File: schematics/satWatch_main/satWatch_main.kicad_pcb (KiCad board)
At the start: 4 copper layers, 45.7 x 28 mm, 55 parts, among them J1 POGO_03x14, J2 Pogo_02x03_UARTPROG, Q1 DMP1045U, Q2 BSS138, Q3 BSS138, SW1 B3U-1000P, SW2 B3U-1000P, SW3 EVQ-P7A01P, SW4 EVQ-P7A01P, SW5 EVQ-P7A01P, U1 PAM2401SCADJ, U2 MIC5365-1.8YC5, U3 ESP32-S3-MINI-1, U4 MAX30101EFD_T, U5 BNO085, U6 DS3231MZ, Y1 32.768Hz

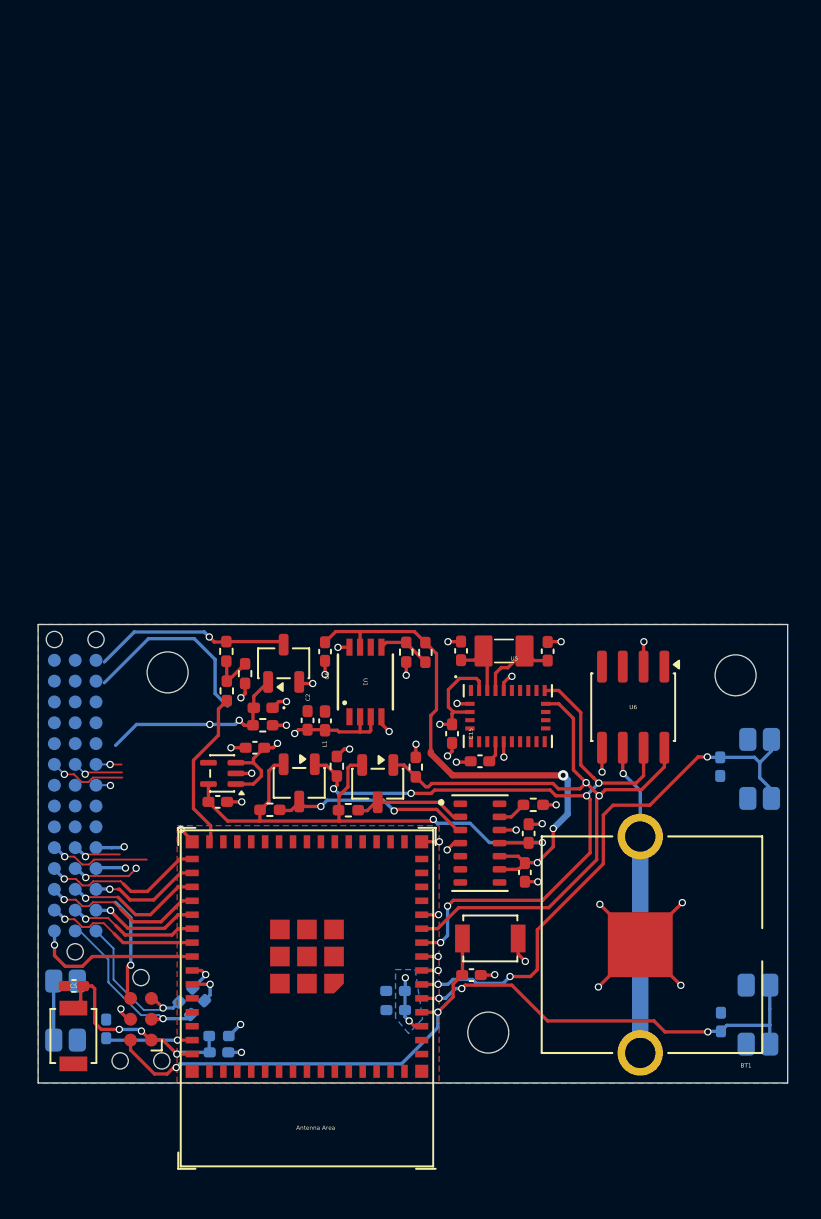
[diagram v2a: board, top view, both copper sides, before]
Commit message: v1
Completed large prototype testing. Implementing post-fab modifications into small-form board. Finalized mainboard routing iterations and added UART programming board.
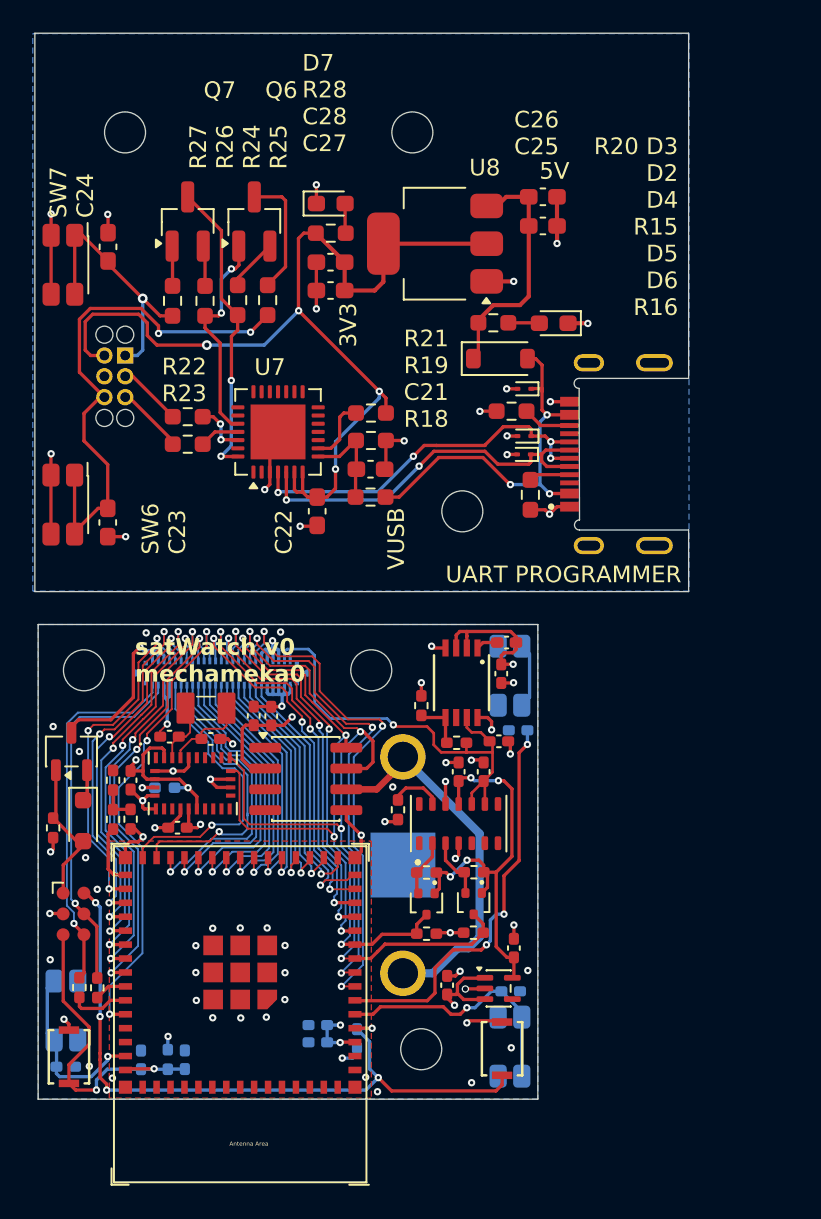
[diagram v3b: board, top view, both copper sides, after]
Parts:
- added C19: 10uF, Capacitor_SMD:C_0402_1005Metric_Pad0.74x0.62mm_HandSolder, F.Cu at (140.2, 81.8)
- added C20: 0.1uF, Capacitor_SMD:C_0402_1005Metric_Pad0.74x0.62mm_HandSolder, F.Cu at (141.2, 81.8)
- added C21: 1uF/16V, Capacitor_SMD:C_0603_1608Metric_Pad1.08x0.95mm_HandSolder, F.Cu at (147.3, 66.7)
- added C22: 10uF/25V, Capacitor_SMD:C_0603_1608Metric_Pad1.08x0.95mm_HandSolder, F.Cu at (144.0, 69.3)
- added C23: 0.1uF/50V, Capacitor_SMD:C_0603_1608Metric_Pad1.08x0.95mm_HandSolder, F.Cu at (131.2, 70.0)
- added C24: 0.1uF/50V, Capacitor_SMD:C_0603_1608Metric_Pad1.08x0.95mm_HandSolder, F.Cu at (131.3, 53.2)
- added C25: 10uF/25V, Capacitor_SMD:C_0603_1608Metric_Pad1.08x0.95mm_HandSolder, F.Cu at (157.8, 51.9)
- added C26: 0.1uF/50V, Capacitor_SMD:C_0603_1608Metric_Pad1.08x0.95mm_HandSolder, F.Cu at (157.8, 50.1)
- added C27: 10uF/25V, Capacitor_SMD:C_0603_1608Metric_Pad1.08x0.95mm_HandSolder, F.Cu at (144.8, 55.8)
- added C28: 0.1uF/50V, Capacitor_SMD:C_0603_1608Metric_Pad1.08x0.95mm_HandSolder, F.Cu at (144.8, 54.1)
- added D2: 1N5819, Diode_SMD:D_SOD-123, F.Cu at (155.2, 60.0)
- added D3: YELLOW, LED_SMD:LED_0603_1608Metric_Pad1.05x0.95mm_HandSolder, F.Cu at (158.4, 57.8)
- added D4: D5V0L1B2S9-7, Diode_SMD:D_SOD-923, F.Cu at (156.7, 61.8)
- added D5: D5V0L1B2S9-7, Diode_SMD:D_SOD-923, F.Cu at (156.7, 64.7)
- added D6: D5V0L1B2S9-7, Diode_SMD:D_SOD-923, F.Cu at (156.6, 65.8)
- added D7: RED, LED_SMD:LED_0603_1608Metric_Pad1.05x0.95mm_HandSolder, F.Cu at (144.8, 50.5)
- added H1: MountingHole, MountingHole:MountingHole_2.5mm, F.Cu at (149.8, 46.2)
- added H2: MountingHole, MountingHole:MountingHole_2.5mm, F.Cu at (132.3, 46.2)
- added H3: MountingHole, MountingHole:MountingHole_2.5mm, F.Cu at (152.9, 69.3)
- added J3: 855-22-006-10-001101, footprint:8552200610001101, B.Cu at (131.7, 61.1)
- added J4: UJ20-C-H-G-MSMT-2B-P16-TR, footprint:SAMESKY_UJ20-C-H-G-MSMT-2B-P16-TR, F.Cu at (163.4, 65.8)
- added Q6: S8050, Package_TO_SOT_SMD:SOT-23_Handsoldering, F.Cu at (140.2, 51.6)
- added Q7: S8050, Package_TO_SOT_SMD:SOT-23_Handsoldering, F.Cu at (136.1, 51.6)
- added R15: 5K, Resistor_SMD:R_0603_1608Metric_Pad0.98x0.95mm_HandSolder, F.Cu at (155.9, 63.2)
- added R16: 5K, Resistor_SMD:R_0603_1608Metric_Pad0.98x0.95mm_HandSolder, F.Cu at (157.0, 68.3)
- added R17: 10K, Resistor_SMD:R_0402_1005Metric_Pad0.72x0.64mm_HandSolder, B.Cu at (134.7, 86.2)
- added R18: 22.1K, Resistor_SMD:R_0603_1608Metric_Pad0.98x0.95mm_HandSolder, F.Cu at (147.3, 68.4)
- added R19: 47.5K, Resistor_SMD:R_0603_1608Metric_Pad0.98x0.95mm_HandSolder, F.Cu at (147.3, 65.0)
- added R20: 5.1K(1%), Resistor_SMD:R_0603_1608Metric_Pad0.98x0.95mm_HandSolder, F.Cu at (154.8, 57.8)
- added R21: 1K, Resistor_SMD:R_0603_1608Metric_Pad0.98x0.95mm_HandSolder, F.Cu at (147.3, 63.3)
- added R22: 0, Resistor_SMD:R_0603_1608Metric_Pad0.98x0.95mm_HandSolder, F.Cu at (136.1, 63.5)
- added R23: 0, Resistor_SMD:R_0603_1608Metric_Pad0.98x0.95mm_HandSolder, F.Cu at (136.1, 65.2)
- added R24: 10K, Resistor_SMD:R_0603_1608Metric_Pad0.98x0.95mm_HandSolder, F.Cu at (139.2, 56.4)
- added R25: 0, Resistor_SMD:R_0603_1608Metric_Pad0.98x0.95mm_HandSolder, F.Cu at (141.0, 56.4)
- added R26: 10K, Resistor_SMD:R_0603_1608Metric_Pad0.98x0.95mm_HandSolder, F.Cu at (137.2, 56.5)
- added R27: 0, Resistor_SMD:R_0603_1608Metric_Pad0.98x0.95mm_HandSolder, F.Cu at (135.2, 56.5)
- added R28: 5.1K, Resistor_SMD:R_0603_1608Metric_Pad0.98x0.95mm_HandSolder, F.Cu at (144.9, 52.3)
- added SW6: EVQ-P7A01P, Button_Switch_SMD:SW_SPST_EVQP7A, F.Cu at (128.5, 68.9)
- added SW7: EVQ-P7A01P, Button_Switch_SMD:SW_SPST_EVQP7A, F.Cu at (128.5, 54.3)
- added U7: CP2102N-Axx-xQFN28, Package_DFN_QFN:QFN-28-1EP_5x5mm_P0.5mm_EP3.35x3.35mm, F.Cu at (141.6, 64.5)
- added U8: AMS1117-3.3, Package_TO_SOT_SMD:SOT-223-3_TabPin2, F.Cu at (151.2, 53.0)
- BT1, C3, C5: moved to B.Cu
- D1: value SS34 -> SDB14HS-AQ; footprint Diode_SMD:D_0402_1005Metric_Pad0.77x0.64mm_HandSolder -> Diode_SMD:D_SOD-323_HandSoldering
- J1: value POGO_03x14 -> Conn_02x25_Top_Bottom; footprint footprint:CUSTOM_POGO_02X21 -> footprint:CON_2167010509_MOL
- Q2, Q3: value BSS138 -> RE1C002UN; footprint Package_TO_SOT_SMD:SOT-23-3 -> Package_TO_SOT_SMD:SOT-416
- R13: value 0 -> 499; moved to F.Cu
- R14: moved to F.Cu
- SW1, SW2: value B3U-1000P -> R-667995; footprint Button_Switch_SMD:SW_SPST_B3U-1000P -> footprint:R-667995_MIT-L
- moved H2 39.8 mm to (129.8, 79.0)
- moved U2 21.4 mm to (155.1, 98.4), turned to 0 degrees
- moved C17 21.2 mm to (137.5, 83.2), turned to 0 degrees
- moved U6 20.4 mm to (143.3, 85.6), turned to 0 degrees
- moved C4 20.1 mm to (156.0, 95.9), turned to 90 degrees
- moved C15 19.8 mm to (132.6, 85.7)
- moved U5 19.6 mm to (136.4, 85.9)
- moved C16 18.9 mm to (135.5, 88.6), turned to 0 degrees
- moved C1 18.6 mm to (151.9, 98.2), turned to 90 degrees
- moved C18 18.5 mm to (135.0, 83.0), turned to 180 degrees
- moved Y1 18.5 mm to (137.2, 81.3)
- moved SW5 16.3 mm to (155.8, 79.3)
- moved BT1 15.3 mm to (149.2, 90.9), turned to -90 degrees
- moved SW3 15.3 mm to (155.8, 102.0)
- moved R1 14.2 mm to (127.9, 88.6), turned to -90 degrees
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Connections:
- net /GPIO0/BOOT renamed /Mainboard/GPIO0/BOOT
- net /GPIO1/BUTTON1 renamed /Mainboard/GPIO1/BUTTON1
- net /GPIO2/BUTTON3 renamed /Mainboard/GPIO2/BUTTON3
- net /GPIO46/BUTTON2 renamed /Mainboard/GPIO46/BUTTON2
- C5 pad 1: /EN/CHIP_PU -> /Mainboard/EN/CHIP_PU
- C7 pad 1: /EN/CHIP_PU -> /Mainboard/EN/CHIP_PU
- J1 pad 1: /BAT+ -> /Mainboard/U0RXD
- J1 pad 10: unconnected-(J1-Pin_10-Pad10) -> /Mainboard/GPIO21
- J1 pad 11: /GPIO4 -> /Mainboard/GPIO20/USBD+
- J1 pad 12: /GPIO36 -> /Mainboard/GPIO19/USBD-
- J1 pad 13: /GPIO39 -> /Mainboard/GPIO18
- J1 pad 14: /U0TXD -> /Mainboard/GPIO17
- J1 pad 15: unconnected-(J1-Pin_15-Pad15) -> /Mainboard/GPIO16
- J1 pad 16: unconnected-(J1-Pin_16-Pad16) -> /Mainboard/GPIO15
- J1 pad 17: unconnected-(J1-Pin_17-Pad17) -> /Mainboard/GPIO14
- J1 pad 18: unconnected-(J1-Pin_18-Pad18) -> /Mainboard/GPIO13
- J1 pad 19: unconnected-(J1-Pin_19-Pad19) -> /Mainboard/GPIO12
- J1 pad 2: 3V3 -> /Mainboard/U0TXD
- J1 pad 20: unconnected-(J1-Pin_20-Pad20) -> /Mainboard/GPIO11
- J1 pad 21: unconnected-(J1-Pin_21-Pad21) -> GND
- J1 pad 22: unconnected-(J1-Pin_22-Pad22) -> GND
- J1 pad 23: unconnected-(J1-Pin_23-Pad23) -> GND
- J1 pad 24: unconnected-(J1-Pin_24-Pad24) -> GND
- J1 pad 25: /GPIO3 -> GND
- J1 pad 26: /GPIO37 -> /Mainboard/BAT+
- J1 pad 27: /GPIO40 -> /Mainboard/BAT+
- J1 pad 28: /U0RXD -> /Mainboard/BAT+
- J1 pad 29: unconnected-(J1-Pin_29-Pad29) -> /Mainboard/GPIO36
- J1 pad 3: unconnected-(J1-Pin_3-Pad3) -> GND
- J1 pad 30: unconnected-(J1-Pin_30-Pad30) -> /Mainboard/GPIO37
- J1 pad 31: unconnected-(J1-Pin_31-Pad31) -> /Mainboard/GPIO38
- J1 pad 32: unconnected-(J1-Pin_32-Pad32) -> /Mainboard/GPIO39
- J1 pad 33: unconnected-(J1-Pin_33-Pad33) -> /Mainboard/GPIO40
- J1 pad 34: unconnected-(J1-Pin_34-Pad34) -> /Mainboard/GPIO41
- J1 pad 35: unconnected-(J1-Pin_35-Pad35) -> /Mainboard/GPIO42
- J1 pad 36: unconnected-(J1-Pin_36-Pad36) -> /Mainboard/GPIO45
- J1 pad 37: unconnected-(J1-Pin_37-Pad37) -> /Mainboard/GPIO10
- J1 pad 38: /GPIO2 -> /Mainboard/GPIO9/MOSI
- J1 pad 39: /GPIO35 -> /Mainboard/GPIO8/MISO
- J1 pad 4: unconnected-(J1-Pin_4-Pad4) -> GND
- J1 pad 40: /GPIO38 -> /Mainboard/GPIO7/SCK
- J1 pad 41: /GPIO41 -> /Mainboard/GPIO6/SCL
- J1 pad 42: /GPIO42 -> /Mainboard/GPIO5/SDA
- J1 pad 5: unconnected-(J1-Pin_5-Pad5) -> /Mainboard/GPIO48
- J1 pad 6: unconnected-(J1-Pin_6-Pad6) -> /Mainboard/GPIO34
- J1 pad 7: unconnected-(J1-Pin_7-Pad7) -> /Mainboard/GPIO33
- J1 pad 8: unconnected-(J1-Pin_8-Pad8) -> /Mainboard/GPIO47
- J1 pad 9: unconnected-(J1-Pin_9-Pad9) -> /Mainboard/GPIO27
- J2 pad 1: /EN/CHIP_PU -> VIN_3V3
- J2 pad 2: /U0RXD -> GND
- J2 pad 3: /U0TXD -> /Mainboard/EN/CHIP_PU
- J2 pad 4: VIN_3V3 -> /Mainboard/U0RXD
- J2 pad 5: GND -> /Mainboard/U0TXD
- Q1 pad 3: /BAT+ -> /Mainboard/BAT+
- Q2 pad 1: /GPIO6/SCL -> 1V8
- Q2 pad 2: 1V8 -> /Mainboard/LV_SCL
- Q2 pad 3: /LV_SCL -> /Mainboard/GPIO6/SCL
- Q3 pad 1: /GPIO5/SDA -> 1V8
- Q3 pad 2: 1V8 -> /Mainboard/LV_SDA
- Q3 pad 3: /LV_SDA -> /Mainboard/GPIO5/SDA
- R11 pad 2: /GPIO5/SDA -> /Mainboard/GPIO5/SDA
- R13 pad 2: /U0TXD -> /Mainboard/U0TXD
- R14 pad 2: /U0RXD -> /Mainboard/U0RXD
- R4 pad 2: /LV_SCL -> /Mainboard/LV_SCL
- R5 pad 2: /EN/CHIP_PU -> /Mainboard/EN/CHIP_PU
- R6 pad 2: /GPIO6/SCL -> /Mainboard/GPIO6/SCL
- R7 pad 1: /GPIO48/BATTERY_MONITOR -> /Mainboard/GPIO35/BATTERY_MONITOR
- R8 pad 2: /BAT+ -> /Mainboard/BAT+
- R9 pad 2: /LV_SDA -> /Mainboard/LV_SDA
- SW2 pad 2: /EN/CHIP_PU -> /Mainboard/EN/CHIP_PU
- U3 pad 10: /GPIO6/SCL -> /Mainboard/GPIO6/SCL
- U3 pad 11: /GPIO7/SCK -> /Mainboard/GPIO7/SCK
- U3 pad 12: /GPIO8/MISO -> /Mainboard/GPIO8/MISO
- U3 pad 13: /GPIO9/MOSI -> /Mainboard/GPIO9/MOSI
- U3 pad 14: /GPIO10 -> /Mainboard/GPIO10
- U3 pad 15: /GPIO11 -> /Mainboard/GPIO11
- U3 pad 16: /GPIO12 -> /Mainboard/GPIO12
- U3 pad 17: /GPIO13 -> /Mainboard/GPIO13
- U3 pad 18: /GPIO14 -> /Mainboard/GPIO14
- U3 pad 19: /GPIO15 -> /Mainboard/GPIO15
- U3 pad 20: /GPIO16 -> /Mainboard/GPIO16
- U3 pad 21: /GPIO17 -> /Mainboard/GPIO17
- U3 pad 22: /GPIO18 -> /Mainboard/GPIO18
- U3 pad 23: /GPIO19/USBD- -> /Mainboard/GPIO19/USBD-
- U3 pad 24: /GPIO20/USBD+ -> /Mainboard/GPIO20/USBD+
- U3 pad 25: /GPIO21 -> /Mainboard/GPIO21
- U3 pad 26: /GPIO27 -> /Mainboard/GPIO27
- U3 pad 27: /GPIO47 -> /Mainboard/GPIO47
- U3 pad 28: /GPIO33 -> /Mainboard/GPIO33
- U3 pad 29: /GPIO34 -> /Mainboard/GPIO34
- U3 pad 30: /GPIO48/BATTERY_MONITOR -> /Mainboard/GPIO48
- U3 pad 31: /GPIO35 -> /Mainboard/GPIO35/BATTERY_MONITOR
- U3 pad 32: /GPIO36 -> /Mainboard/GPIO36
- U3 pad 33: /GPIO37 -> /Mainboard/GPIO37
- U3 pad 34: /GPIO38 -> /Mainboard/GPIO38
- U3 pad 35: /GPIO39 -> /Mainboard/GPIO39
- U3 pad 36: /GPIO40 -> /Mainboard/GPIO40
- U3 pad 37: /GPIO41 -> /Mainboard/GPIO41
- U3 pad 38: /GPIO42 -> /Mainboard/GPIO42
- U3 pad 41: /GPIO45 -> /Mainboard/GPIO45
- U3 pad 45: /EN/CHIP_PU -> /Mainboard/EN/CHIP_PU
- U3 pad 7: /GPIO3 -> /Mainboard/GPIO3
- U3 pad 8: /GPIO4 -> /Mainboard/GPIO4
- U3 pad 9: /GPIO5/SDA -> /Mainboard/GPIO5/SDA
- U4 pad 2: /LV_SCL -> /Mainboard/LV_SCL
- U4 pad 3: /LV_SDA -> /Mainboard/LV_SDA
- U5 pad 11: unconnected-(U5-~{RST}-Pad11) -> 3V3
- U5 pad 17: unconnected-(U5-SA0/H_MOSI-Pad17) -> GND
- U5 pad 18: unconnected-(U5-~{H_CS}-Pad18) -> GND
- U5 pad 19: /GPIO6/SCL -> /Mainboard/GPIO6/SCL
- U5 pad 20: /GPIO5/SDA -> /Mainboard/GPIO5/SDA
- U5 pad 4: unconnected-(U5-~{BOOT}-Pad4) -> Net-(U5-~{BOOT})
- U5 pad 5: unconnected-(U5-PS1-Pad5) -> GND
- U5 pad 6: unconnected-(U5-PS0/WAKE-Pad6) -> GND
- U6 pad 7: /GPIO5/SDA -> /Mainboard/GPIO5/SDA
- U6 pad 8: /GPIO6/SCL -> /Mainboard/GPIO6/SCL
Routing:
- net PROG_3V3: track 0.00 -> 60.1 mm, vias 0 -> 4
- net /Mainboard/GPIO5/SDA: track 0.00 -> 52.6 mm, vias 0 -> 4
- net /GPIO5/SDA: track 49.6 -> 0.00 mm, vias 6 -> 0
- net /GPIO6/SCL: track 42.4 -> 0.00 mm, vias 2 -> 0
- net /Mainboard/GPIO6/SCL: track 0.00 -> 41.6 mm, vias 0 -> 4
- net PROG_GND: track 0.00 -> 36.3 mm, vias 0 -> 18
- net /Programmer/EN/CHIP_PU: track 0.00 -> 32.9 mm, vias 0 -> 2
- net /Mainboard/GPIO3: track 0.00 -> 31.3 mm, vias 0 -> 3
- net /Mainboard/GPIO45: track 0.00 -> 29.8 mm, vias 0 -> 3
- net /Mainboard/GPIO4: track 0.00 -> 29.1 mm, vias 0 -> 3
- net /Mainboard/GPIO42: track 0.00 -> 26.2 mm, vias 0 -> 3
- net /Mainboard/GPIO41: track 0.00 -> 26.0 mm, vias 0 -> 3
- net /Mainboard/GPIO7/SCK: track 0.00 -> 25.1 mm, vias 0 -> 3
- net /Mainboard/GPIO40: track 0.00 -> 24.3 mm, vias 0 -> 3
- net /Mainboard/GPIO39: track 0.00 -> 24.1 mm, vias 0 -> 3
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- added copper zone on In2.Cu, net PROG_3V3
- added copper zone on B.Cu, net PROG_GND
- added copper zone on In1.Cu, net PROG_GND
- removed copper zone on B.Cu, net (none)
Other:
- board size 45.7 x 28 mm -> 39.9 x 65 mm
- board text added: "3V3"
- board text added: "5V"
- board text added: "BOOT 3V3 TX GND RX EN"
- board text added: "C22"
- board text added: "C26 C25"
- board text added: "D7 R28 C28 C27"
- board text added: "MAINBOARD"
- board text added: "Q7 Q6"
- board text added: "R20 D3 D2 D4 R15 D5 D6 R16"
- board text added: "R21 R19 C21 R18"
- board text added: "R22 R23"
- board text added: "R27 R26 R24 R25"
- board text added: "SW6 C23"
- board text added: "SW7 C24"
- board text added: "U7"
- board text added: "U8"
- board text added: "UART PROGRAMMER"
- board text added: "VUSB"
- board text added: "satWatch v0 mechameka0"

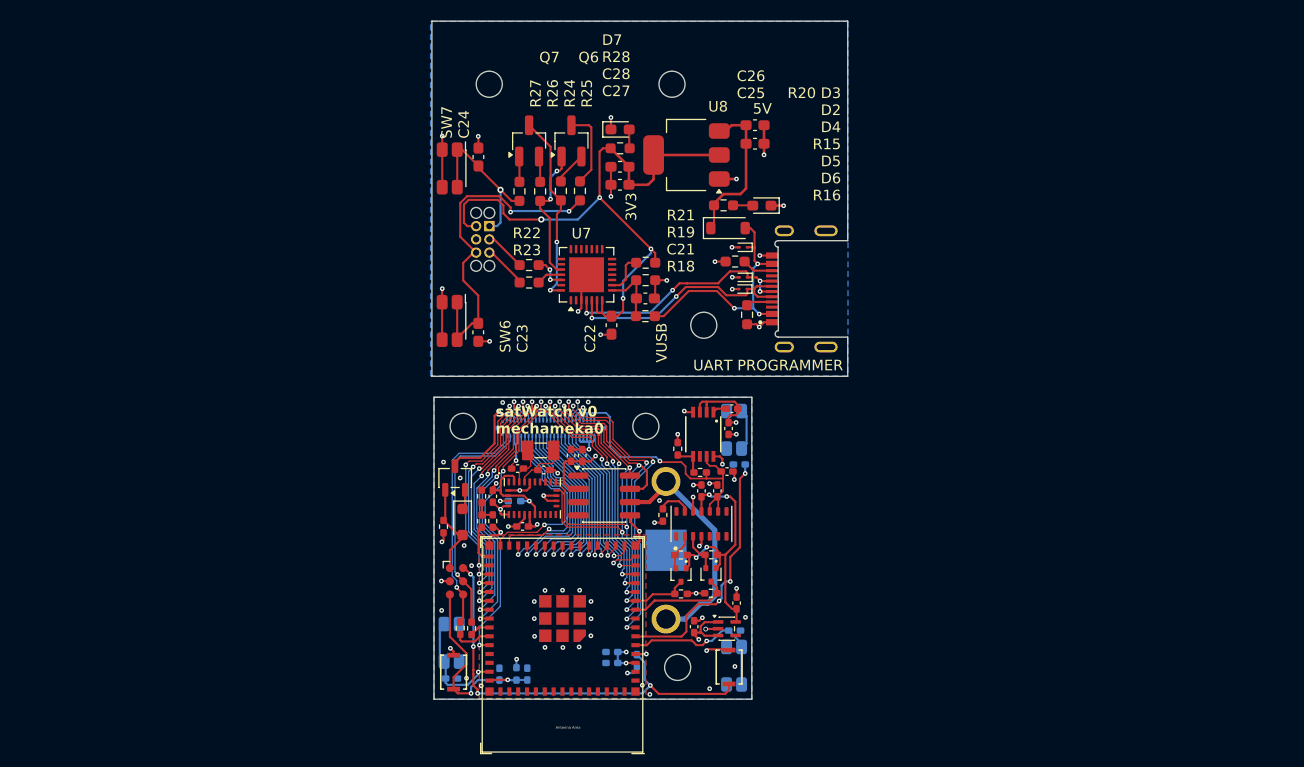
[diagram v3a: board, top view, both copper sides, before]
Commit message: v1.1
Completed board layout for charging dock configuration and a default watchface config
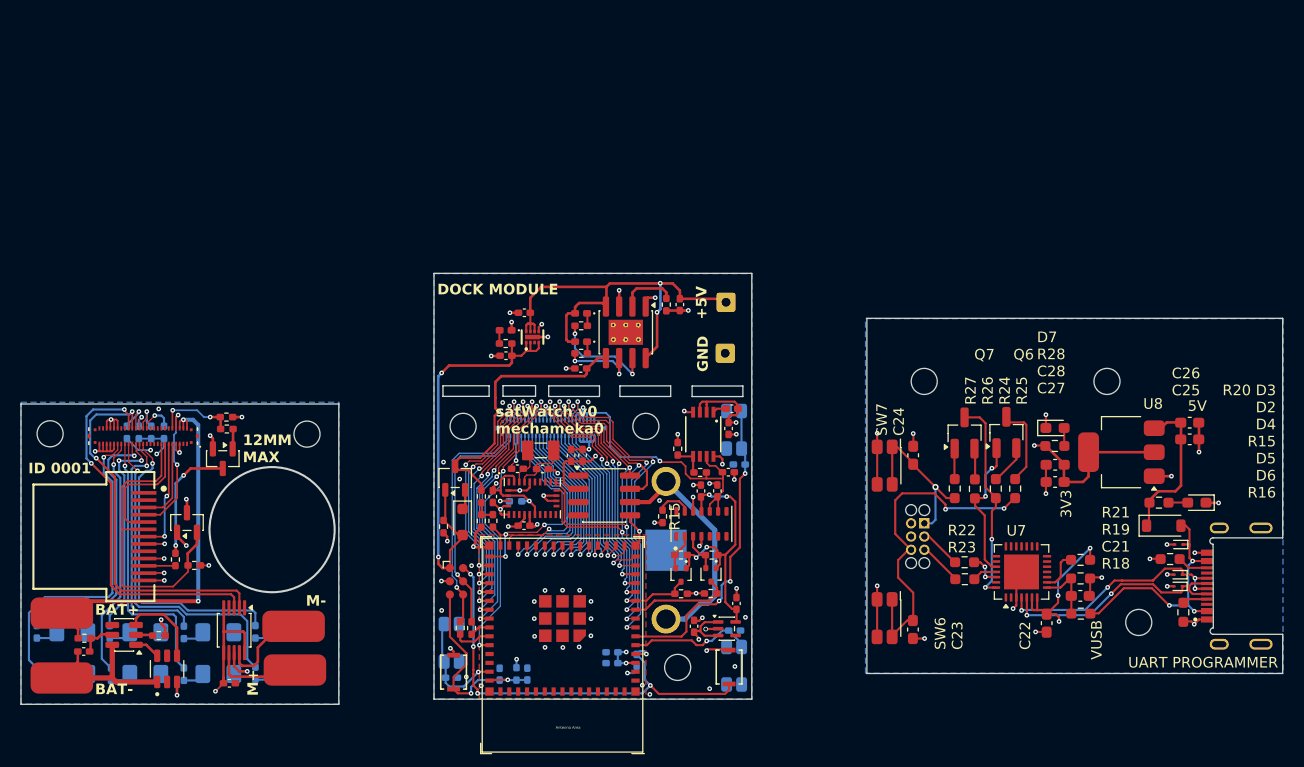
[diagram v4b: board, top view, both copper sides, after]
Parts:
- added C29: 0.1uF, Capacitor_SMD:C_0402_1005Metric_Pad0.74x0.62mm_HandSolder, F.Cu at (150.6, 67.3)
- added C30: 10uF, Capacitor_SMD:C_0402_1005Metric_Pad0.74x0.62mm_HandSolder, F.Cu at (141.1, 73.4)
- added C31: 1uF, Capacitor_SMD:C_0402_1005Metric_Pad0.74x0.62mm_HandSolder, F.Cu at (135.7, 68.1)
- added C32: 1uF, Capacitor_SMD:C_0402_1005Metric_Pad0.74x0.62mm_HandSolder, F.Cu at (133.9, 72.2)
- added C33: 1uF, Capacitor_SMD:C_0402_1005Metric_Pad0.74x0.62mm_HandSolder, F.Cu at (107.4, 103.6)
- added C34: 0.1uF, Capacitor_SMD:C_0402_1005Metric_Pad0.74x0.62mm_HandSolder, F.Cu at (93.4, 100.6)
- added D10: RED, LED_SMD:LED_0402_1005Metric_Pad0.77x0.64mm_HandSolder, F.Cu at (133.9, 69.8)
- added D11: LED, LED_SMD:LED_1206_3216Metric_Pad1.42x1.75mm_HandSolder, B.Cu at (113.3, 98.7)
- added D12: LED, LED_SMD:LED_1206_3216Metric_Pad1.42x1.75mm_HandSolder, B.Cu at (106.3, 98.7)
- added D13: LED, LED_SMD:LED_1206_3216Metric_Pad1.42x1.75mm_HandSolder, B.Cu at (99.3, 98.7)
- added D14: LED, LED_SMD:LED_1206_3216Metric_Pad1.42x1.75mm_HandSolder, B.Cu at (92.3, 98.7)
- added D15: LED, LED_SMD:LED_1206_3216Metric_Pad1.42x1.75mm_HandSolder, B.Cu at (113.3, 102.7)
- added D16: LED, LED_SMD:LED_1206_3216Metric_Pad1.42x1.75mm_HandSolder, B.Cu at (106.3, 102.7)
- added D17: LED, LED_SMD:LED_1206_3216Metric_Pad1.42x1.75mm_HandSolder, B.Cu at (99.3, 102.7)
- added D18: LED, LED_SMD:LED_1206_3216Metric_Pad1.42x1.75mm_HandSolder, B.Cu at (92.3, 102.7)
- added D8: DONE, LED_SMD:LED_0402_1005Metric_Pad0.77x0.64mm_HandSolder, F.Cu at (141.1, 70.9)
- added D9: CHRG, LED_SMD:LED_0402_1005Metric_Pad0.77x0.64mm_HandSolder, F.Cu at (141.1, 68.2)
- added H1: MountingHole, MountingHole:MountingHole_2.5mm, F.Cu at (114.8, 79.7)
- added H2: MountingHole, MountingHole:MountingHole_2.5mm, F.Cu at (90.2, 79.7)
- added J10: BAT+, Connector_Wire:SolderWirePad_1x01_SMD_3x6mm, F.Cu at (91.3, 96.9)
- added J11: BAT-, Connector_Wire:SolderWirePad_1x01_SMD_3x6mm, F.Cu at (91.3, 103.1)
- added J5: SOLDER POINT, Connector_Wire:SolderWire-0.25sqmm_1x01_D0.65mm_OD1.7mm, F.Cu at (155.0, 67.1)
- added J6: SOLDER POINT, Connector_Wire:SolderWire-0.25sqmm_1x01_D0.65mm_OD1.7mm, F.Cu at (154.9, 72.0)
- added J7: 2167010509_MOLEX, footprint:CON_2167010509_MOL, F.Cu at (99.1, 79.9)
- added J8: MOTOR+, Connector_Wire:SolderWirePad_1x01_SMD_3x6mm, F.Cu at (113.7, 102.4)
- added J9: MOTOR-, Connector_Wire:SolderWirePad_1x01_SMD_3x6mm, F.Cu at (113.5, 98.2)
- added Q4: S8050, Package_TO_SOT_SMD:SOT-23_Handsoldering, F.Cu at (181.9, 79.6)
- added Q5: S8050, Package_TO_SOT_SMD:SOT-23_Handsoldering, F.Cu at (177.9, 79.6)
- added R29: 1K, Resistor_SMD:R_0402_1005Metric_Pad0.72x0.64mm_HandSolder, F.Cu at (141.1, 72.0)
- added R30: 1K, Resistor_SMD:R_0402_1005Metric_Pad0.72x0.64mm_HandSolder, F.Cu at (141.1, 69.4)
- added R31: 1.2k, Resistor_SMD:R_0402_1005Metric_Pad0.72x0.64mm_HandSolder, F.Cu at (149.3, 67.3)
- added R32: 5.1K(1%), Resistor_SMD:R_0402_1005Metric_Pad0.72x0.64mm_HandSolder, F.Cu at (133.9, 71.1)
- added R33: 1K, Resistor_SMD:R_0402_1005Metric_Pad0.72x0.64mm_HandSolder, F.Cu at (107.1, 79.2)
- added R34: 22, Resistor_SMD:R_0402_1005Metric_Pad0.72x0.64mm_HandSolder, F.Cu at (102.2, 91.8)
- added R35: 10K, Resistor_SMD:R_0402_1005Metric_Pad0.72x0.64mm_HandSolder, F.Cu at (107.1, 78.1)
- added R36: 10K, Resistor_SMD:R_0402_1005Metric_Pad0.72x0.64mm_HandSolder, F.Cu at (104.0, 92.3)
- added R37: 180, Resistor_SMD:R_0402_1005Metric_Pad0.72x0.64mm_HandSolder, B.Cu at (109.9, 98.7)
- added R38: 180, Resistor_SMD:R_0402_1005Metric_Pad0.72x0.64mm_HandSolder, B.Cu at (103.0, 98.7)
- added R39: 180, Resistor_SMD:R_0402_1005Metric_Pad0.72x0.64mm_HandSolder, B.Cu at (95.9, 98.7)
- added R40: 180, Resistor_SMD:R_0402_1005Metric_Pad0.72x0.64mm_HandSolder, B.Cu at (88.9, 98.7)
- added R41: 180, Resistor_SMD:R_0402_1005Metric_Pad0.72x0.64mm_HandSolder, B.Cu at (109.9, 102.7)
- added R42: 180, Resistor_SMD:R_0402_1005Metric_Pad0.72x0.64mm_HandSolder, B.Cu at (103.0, 102.8)
- added R43: 180, Resistor_SMD:R_0402_1005Metric_Pad0.72x0.64mm_HandSolder, B.Cu at (96.0, 102.8)
- added R44: 180, Resistor_SMD:R_0402_1005Metric_Pad0.72x0.64mm_HandSolder, B.Cu at (88.9, 102.8)
- added R45: 100, Resistor_SMD:R_0402_1005Metric_Pad0.72x0.64mm_HandSolder, F.Cu at (93.5, 99.3)
- added R46: 1K, Resistor_SMD:R_0402_1005Metric_Pad0.72x0.64mm_HandSolder, F.Cu at (100.6, 99.1)
- added R47: 10K, Resistor_SMD:R_0402_1005Metric_Pad0.72x0.64mm_HandSolder, B.Cu at (97.6, 79.6)
- added R48: 10K, Resistor_SMD:R_0402_1005Metric_Pad0.72x0.64mm_HandSolder, B.Cu at (98.7, 79.6)
- added R49: 10K, Resistor_SMD:R_0402_1005Metric_Pad0.72x0.64mm_HandSolder, B.Cu at (99.9, 79.6)
- added R50: 10K, Resistor_SMD:R_0402_1005Metric_Pad0.72x0.64mm_HandSolder, B.Cu at (101.1, 79.6)
- added U10: NCP186AMX330TAG, footprint:PSON40P160X120X45-9N, F.Cu at (136.4, 70.4)
- added U11: ~, footprint:Wisevision N096-1608TBBIG11-H13, F.Cu at (99.2, 89.6)
- added U12: ~, Package_TO_SOT_SMD:SOT-23, F.Cu at (103.3, 88.2)
- added U13: DRV2605LDGS, Package_SO:TSSOP-10_3x3mm_P0.5mm, F.Cu at (107.8, 98.5)
- added U14: DW01A, Package_TO_SOT_SMD:SOT-23-6, F.Cu at (97.3, 99.0)
- added U9: TP4056-42-ESOP8, Package_SO:SOIC-8-1EP_3.9x4.9mm_P1.27mm_EP2.41x3.3mm_ThermalVias, F.Cu at (145.4, 70.0)
- C12: value 0.1uF/50V(10%) -> 0.1uF; moved to F.Cu
- C13: value 0.1uF -> 0.1uF/50V(10%); moved to B.Cu
- C17: value 22pF -> 10uF
- C19: value 10uF -> 0.1uF
- C20: value 0.1uF -> 22pF
- C21: value 1uF/16V -> 10uF/25V
- C22, C27: value 10uF/25V -> 0.1uF/50V
- C23, C26: value 0.1uF/50V -> 10uF/25V
- C25: value 10uF/25V -> 1uF/16V
- C3: value 0.1uF/50V(10%) -> 1uF; moved to F.Cu
- C4: value 1uF -> 22uF
- C5: value 0.1uF/50V(10%) -> 1uF/16V(10%)
- C6: value 22uF -> 10uF/16V(10%); moved to B.Cu
- C8: value 1uF/16V(10%) -> 0.1uF/50V(10%)
- C9: value 10uF/16V(10%) -> 0.1uF/50V(10%)
- D2: value 1N5819 -> D5V0L1B2S9-7; footprint Diode_SMD:D_SOD-123 -> Diode_SMD:D_SOD-923
- D3: value YELLOW -> D5V0L1B2S9-7; footprint LED_SMD:LED_0603_1608Metric_Pad1.05x0.95mm_HandSolder -> Diode_SMD:D_SOD-923
- D4: value D5V0L1B2S9-7 -> 1N5819; footprint Diode_SMD:D_SOD-923 -> Diode_SMD:D_SOD-123
- D6: value D5V0L1B2S9-7 -> RED; footprint Diode_SMD:D_SOD-923 -> LED_SMD:LED_0603_1608Metric_Pad1.05x0.95mm_HandSolder
- D7: value RED -> YELLOW
- J1: value Conn_02x25_Top_Bottom -> 2167010509_MOLEX
- Q6: value S8050 -> MMBT2222A; footprint Package_TO_SOT_SMD:SOT-23_Handsoldering -> Package_TO_SOT_SMD:SOT-23
- Q7: value S8050 -> FS8205; footprint Package_TO_SOT_SMD:SOT-23_Handsoldering -> footprint:SOT95P280X145-6N
- R12: value 4.7K -> 220K
- R13: value 499 -> 2.2K
- R14: value 0 -> 10K; moved to B.Cu
- R15: value 5K -> 4.7K; footprint Resistor_SMD:R_0603_1608Metric_Pad0.98x0.95mm_HandSolder -> Resistor_SMD:R_0402_1005Metric_Pad0.72x0.64mm_HandSolder
- R17: value 10K -> 5K; footprint Resistor_SMD:R_0402_1005Metric_Pad0.72x0.64mm_HandSolder -> Resistor_SMD:R_0603_1608Metric_Pad0.98x0.95mm_HandSolder; moved to F.Cu
- R18: value 22.1K -> 5.1K
- R19: value 47.5K -> 5.1K(1%)
- R20: value 5.1K(1%) -> 22.1K
- R21: value 1K -> 47.5K
- R22: value 0 -> 1K
- R23: value 0 -> 10K
- R26: value 10K -> 0
- R28: value 5.1K -> 0
- R6: value 2.2K -> 499
- R8: value 220K -> 2.2K
- R9: value 2.2K -> 0
- moved D7 65.9 mm to (200.2, 86.3), turned to 180 degrees
- moved R17 65.0 mm to (198.9, 96.8), turned to -90 degrees
- moved C24 63.5 mm to (186.6, 84.3), turned to 180 degrees
- moved Q7 61.4 mm to (101.4, 102.2)
- moved R22 60.0 mm to (189.0, 91.8)
- moved C23 56.8 mm to (186.6, 82.7), turned to 180 degrees
- moved C22 56.2 mm to (199.5, 78.6), turned to 0 degrees
- moved R27 55.4 mm to (182.7, 85.0)
- moved C26 55.3 mm to (185.8, 97.9), turned to 90 degrees
- moved R26 55.2 mm to (177.9, 93.7), turned to 0 degrees
- moved C21 53.9 mm to (199.5, 80.2)
- moved R19 53.7 mm to (196.5, 86.3), turned to 180 degrees
- moved C25 53.4 mm to (189.0, 95.3)
- moved D3 53.4 mm to (198.4, 93.2)
- moved D2 52.8 mm to (198.4, 90.3), turned to 180 degrees
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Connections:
- net /Mainboard/GPIO7/SCK renamed /Mainboard/GPIO7
- net /Mainboard/GPIO8/MISO renamed /Mainboard/GPIO8
- net /Mainboard/GPIO9/MOSI renamed /Mainboard/GPIO9
- C12 pad 1: /Mainboard/GPIO46/BUTTON2 -> 1V8
- C13 pad 1: 1V8 -> /Mainboard/GPIO46/BUTTON2
- C15 pad 1: 3V3 -> Net-(U5-CAP)
- C16 pad 1: Net-(U5-CAP) -> 3V3
- C17 pad 1: Net-(U5-XOUT32/CLKSEL1) -> 3V3
- C18 pad 1: Net-(U5-XIN32) -> Net-(U5-XOUT32/CLKSEL1)
- C20 pad 1: 3V3 -> Net-(U5-XIN32)
- C21 pad 1: Net-(U7-VBUS) -> PROG_5V
- C22 pad 1: PROG_GND -> PROG_5V
- C22 pad 2: PROG_3V3 -> PROG_GND
- C23 pad 1: /Programmer/EN/CHIP_PU -> PROG_3V3
- C24 pad 1: /Programmer/GPIO0/BOOT -> PROG_3V3
- C25 pad 1: PROG_5V -> Net-(U7-VBUS)
- C26 pad 1: PROG_5V -> PROG_GND
- C26 pad 2: PROG_GND -> PROG_3V3
- C27 pad 1: PROG_3V3 -> /Programmer/EN/CHIP_PU
- C28 pad 1: PROG_3V3 -> /Programmer/GPIO0/BOOT
- C3 pad 1: /Mainboard/GPIO0/BOOT -> 1V8
- C4 pad 1: 1V8 -> 5V
- C5 pad 1: /Mainboard/EN/CHIP_PU -> 3V3
- C6 pad 1: 5V -> 3V3
- C8 pad 1: 3V3 -> /Mainboard/GPIO0/BOOT
- C9 pad 1: 3V3 -> /Mainboard/EN/CHIP_PU
- D2 pad 1: PROG_5V -> VUSB
- D2 pad 2: VUSB -> PROG_GND
- D3 pad 1: PROG_GND -> /Programmer/D+
- D3 pad 2: Net-(D3-A) -> PROG_GND
- D4 pad 1: VUSB -> PROG_5V
- D4 pad 2: PROG_GND -> VUSB
- D5 pad 1: /Programmer/D+ -> /Programmer/D-
- D6 pad 1: /Programmer/D- -> PROG_GND
- D6 pad 2: PROG_GND -> Net-(D6-A)
- J1 pad 5: /Mainboard/GPIO48 -> /Mainboard/GPIO35
- Q6 pad 1: /Programmer/RTS -> Net-(Q6-B)
- Q6 pad 2: Net-(Q6-B) -> FRONT_GND
- Q7 pad 1: Net-(Q7-E) -> Net-(J11-Pin_1)
- Q7 pad 2: Net-(Q7-B) -> unconnected-(Q7-Pad2)
- Q7 pad 3: /Programmer/DTR -> FRONT_GND
- R10 pad 2: GND -> /Mainboard/BAT+
- R11 pad 1: 3V3 -> 1V8
- R11 pad 2: /Mainboard/GPIO5/SDA -> /Mainboard/LV_SDA
- R12 pad 1: Net-(U4-~{INT}) -> Net-(R10-Pad1)
- R12 pad 2: 3V3 -> GND
- R13 pad 1: Net-(U3-TXD0) -> 3V3
- R13 pad 2: /Mainboard/U0TXD -> /Mainboard/GPIO5/SDA
- R14 pad 1: Net-(U3-RXD0) -> 3V3
- R14 pad 2: /Mainboard/U0RXD -> Net-(U5-~{BOOT})
- R15 pad 1: Net-(J4-CC2) -> Net-(U4-~{INT})
- R15 pad 2: PROG_GND -> 3V3
- R16 pad 1: Net-(J4-CC1) -> Net-(J4-CC2)
- R17 pad 1: 3V3 -> Net-(J4-CC1)
- R17 pad 2: Net-(U5-~{BOOT}) -> PROG_GND
- R18 pad 1: VUSB -> PROG_3V3
- R18 pad 2: Net-(U7-VBUS) -> Net-(D6-A)
- R19 pad 1: Net-(U7-VBUS) -> Net-(D7-A)
- R19 pad 2: PROG_GND -> PROG_5V
- R20 pad 1: Net-(D3-A) -> VUSB
- R20 pad 2: PROG_5V -> Net-(U7-VBUS)
- R21 pad 1: Net-(U7-~{RST}) -> Net-(U7-VBUS)
- R21 pad 2: PROG_3V3 -> PROG_GND
- R22 pad 1: /Programmer/U0TXD -> Net-(U7-~{RST})
- R22 pad 2: Net-(U7-TXD) -> PROG_3V3
- R23 pad 1: /Programmer/U0RXD -> Net-(Q4-B)
- R23 pad 2: Net-(U7-RXD) -> /Programmer/DTR
- R24 pad 1: Net-(Q6-B) -> Net-(Q5-B)
- R24 pad 2: /Programmer/DTR -> /Programmer/RTS
- R25 pad 1: /Programmer/EN/CHIP_PU -> /Programmer/U0TXD
- R25 pad 2: Net-(Q6-C) -> Net-(U7-TXD)
- R26 pad 1: Net-(Q7-B) -> /Programmer/U0RXD
- R26 pad 2: /Programmer/RTS -> Net-(U7-RXD)
- R27 pad 1: /Programmer/GPIO0/BOOT -> /Programmer/EN/CHIP_PU
- R27 pad 2: Net-(Q7-E) -> Net-(Q4-C)
- R28 pad 1: PROG_3V3 -> /Programmer/GPIO0/BOOT
- R28 pad 2: Net-(D7-A) -> Net-(Q5-E)
- R6 pad 1: 3V3 -> Net-(U3-TXD0)
- R6 pad 2: /Mainboard/GPIO6/SCL -> /Mainboard/U0TXD
- R7 pad 1: /Mainboard/GPIO35/BATTERY_MONITOR -> Net-(U3-RXD0)
- R7 pad 2: Net-(R10-Pad1) -> /Mainboard/U0RXD
- R8 pad 1: Net-(R10-Pad1) -> 3V3
- R8 pad 2: /Mainboard/BAT+ -> /Mainboard/GPIO6/SCL
- R9 pad 1: 1V8 -> /Mainboard/BATTERY_MONITOR
- R9 pad 2: /Mainboard/LV_SDA -> Net-(R10-Pad1)
- U3 pad 30: /Mainboard/GPIO48 -> /Mainboard/BATTERY_MONITOR
- U3 pad 31: /Mainboard/GPIO35/BATTERY_MONITOR -> /Mainboard/GPIO35
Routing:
- net /Mainboard/VDOCK_5V: track 0.00 -> 44.1 mm, vias 0 -> 2
- net /face1/BAT+: track 0.00 -> 38.1 mm, vias 0 -> 2
- net /face1/GPIO6/SCL: track 0.00 -> 36.4 mm, vias 0 -> 2
- net /face1/GPIO5/SDA: track 0.00 -> 36.4 mm, vias 0 -> 2
- net VIN_3V3: track 9.05 -> 42.8 mm, vias 0 -> 2
- net /face1/GPIO14: track 0.00 -> 31.9 mm, vias 0 -> 1
- net /face1/GPIO11: track 0.00 -> 30.0 mm, vias 0 -> 1
- net /face1/GPIO47: track 0.00 -> 30.0 mm
- net /face1/GPIO18: track 0.00 -> 29.0 mm, vias 0 -> 1
- net PROG_3V3: track 60.1 -> 31.3 mm
- net /face1/GPIO15: track 0.00 -> 26.9 mm, vias 0 -> 1
- net FRONT_3V3: track 0.00 -> 26.7 mm, vias 0 -> 8
- net /face1/GPIO13: track 0.00 -> 26.2 mm, vias 0 -> 1
- net FRONT_GND: track 0.00 -> 24.1 mm, vias 0 -> 11
- net /face1/GPIO17: track 0.00 -> 23.4 mm, vias 0 -> 1
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- added copper zone on In2.Cu, net FRONT_3V3
- added copper zone on B.Cu, net FRONT_GND
- added copper zone on In1.Cu, net FRONT_GND
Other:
- board size 39.9 x 65 mm -> 121 x 41.3 mm
- board text added: "+5V"
- board text added: "12MM MAX"
- board text added: "BAT+"
- board text added: "BAT-"
- board text added: "DOCK MODULE"
- board text added: "DOWN DIRECTION --->"
- board text added: "GND"
- board text added: "ID 0001"
- board text added: "IPS 0.96{dblquote} 80*160"
- board text added: "LED 18 17 16 15 14 13 12 11"
- board text added: "M+"
- board text added: "M-"
- board text added: "V-CUTS"
- board text added: "WRIST DIRECTION --->"
